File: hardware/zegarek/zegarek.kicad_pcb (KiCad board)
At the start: 2 copper layers, 123.5 x 51 mm, 15 parts, among them J1 Conn_01x02_Socket, J2 Conn_01x02_Pin, Q1 IRF740, U1 MC34063AD

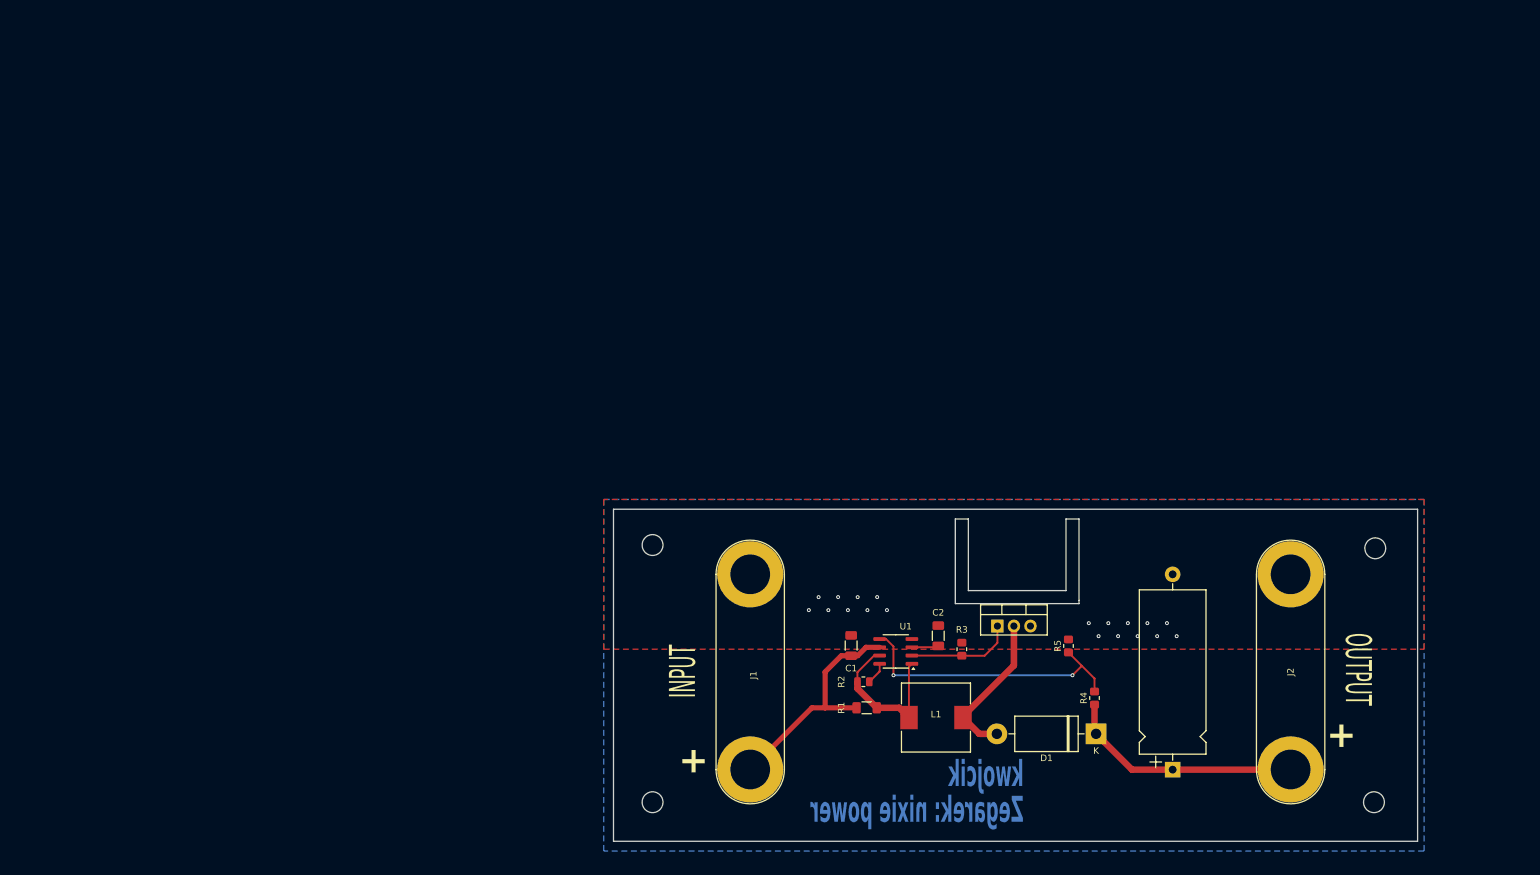
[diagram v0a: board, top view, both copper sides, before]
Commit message: done placing footprins on pcb, started tracing pcb
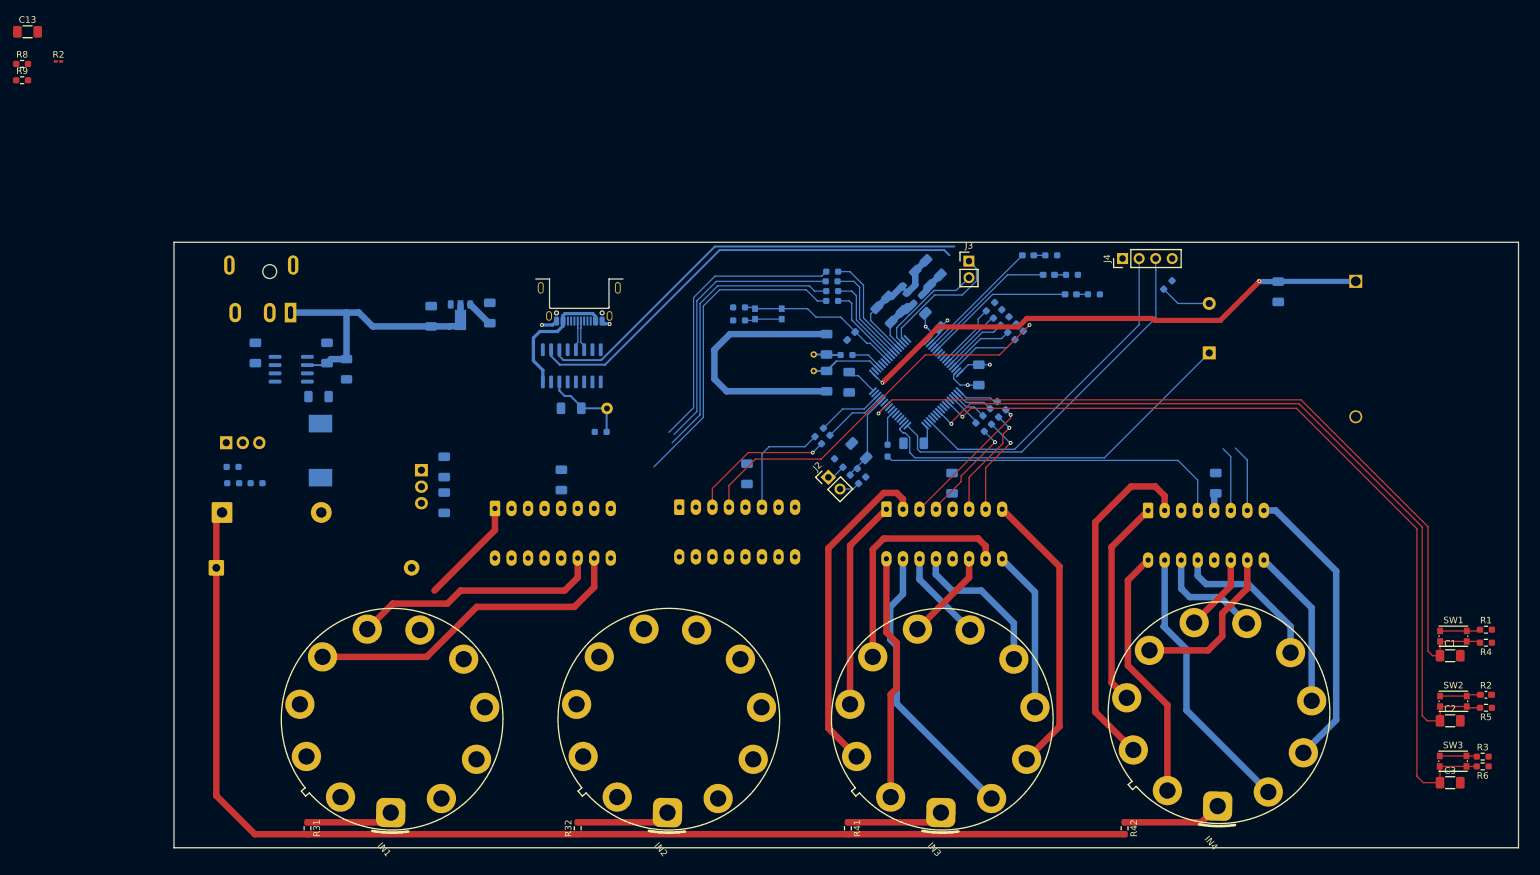
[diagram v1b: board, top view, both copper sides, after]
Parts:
- removed the R2 at (130.9, 101.0)
- removed REF**: SINK, Heatsink:SINK
- added BT1: Battery_Cell, Battery:BatteryHolder_MYOUNG_BS-07-A1BJ001_CR2032, B.Cu at (206.5, 39.5)
- added BZ1: Buzzer, Buzzer_Beeper:MagneticBuzzer_StarMicronics_HMB, B.Cu at (184.0, 50.5)
- added C10: 4u7 250V, Capacitor_THT:CP_Axial_L25.0mm_D10.0mm_P30.00mm_Horizontal, B.Cu at (31.5, 83.5)
- added C11: 10u, Capacitor_SMD:C_1206_3216Metric_Pad1.33x1.80mm_HandSolder, B.Cu at (140.0, 39.0)
- added C12: 100n, Capacitor_SMD:C_1206_3216Metric_Pad1.33x1.80mm_HandSolder, B.Cu at (141.6, 37.4)
- added C13: 100n, Capacitor_SMD:C_1206_3216Metric_Pad1.33x1.80mm_HandSolder, F.Cu at (2.50, 1.18)
- added C13: 100n, Capacitor_SMD:C_0603_1608Metric_Pad1.08x0.95mm_HandSolder, B.Cu at (129.0, 47.9)
- added C14: 100n, Capacitor_SMD:C_1206_3216Metric_Pad1.33x1.80mm_HandSolder, B.Cu at (130.2, 65.5)
- added C15: 10u, Capacitor_SMD:C_1206_3216Metric_Pad1.33x1.80mm_HandSolder, B.Cu at (134.0, 44.7)
- added C16: 100n, Capacitor_SMD:C_1206_3216Metric_Pad1.33x1.80mm_HandSolder, B.Cu at (135.7, 43.0)
- added C17: 4.3p, Capacitor_SMD:C_1206_3216Metric_Pad1.33x1.80mm_HandSolder, B.Cu at (125.2, 54.8)
- added C18: 4.3p, Capacitor_SMD:C_1206_3216Metric_Pad1.33x1.80mm_HandSolder, B.Cu at (125.2, 49.2)
- added C19: 100n, Capacitor_SMD:C_1206_3216Metric_Pad1.33x1.80mm_HandSolder, B.Cu at (194.6, 41.1)
- added C20: 100n, Capacitor_SMD:C_1206_3216Metric_Pad1.33x1.80mm_HandSolder, B.Cu at (128.7, 55.0)
- added C21: 100n, Capacitor_SMD:C_1206_3216Metric_Pad1.33x1.80mm_HandSolder, B.Cu at (138.6, 64.4)
- added C22: 100n, Capacitor_SMD:C_1206_3216Metric_Pad1.33x1.80mm_HandSolder, B.Cu at (141.5, 45.5)
- added C23: 100n, Capacitor_SMD:C_1206_3216Metric_Pad1.33x1.80mm_HandSolder, B.Cu at (148.6, 53.9)
- added C24: 100n, Capacitor_SMD:C_1206_3216Metric_Pad1.33x1.80mm_HandSolder, B.Cu at (86.0, 59.0)
- added C25: 100n, Capacitor_SMD:C_1206_3216Metric_Pad1.33x1.80mm_HandSolder, B.Cu at (84.5, 70.0)
- added C26: 100n, Capacitor_SMD:C_1206_3216Metric_Pad1.33x1.80mm_HandSolder, B.Cu at (113.0, 69.1)
- added C27: 100n, Capacitor_SMD:C_1206_3216Metric_Pad1.33x1.80mm_HandSolder, B.Cu at (144.5, 70.5)
- added C28: 100n, Capacitor_SMD:C_1206_3216Metric_Pad1.33x1.80mm_HandSolder, B.Cu at (185.0, 70.5)
- added C4: 0.33u, Capacitor_SMD:C_1206_3216Metric_Pad1.33x1.80mm_HandSolder, B.Cu at (64.5, 44.9)
- added C5: 100n, Capacitor_SMD:C_1206_3216Metric_Pad1.33x1.80mm_HandSolder, B.Cu at (73.5, 44.4)
- added C6: 100nF, Capacitor_SMD:C_1206_3216Metric_Pad1.33x1.80mm_HandSolder, B.Cu at (48.5, 50.5)
- added C7: 1nF, Capacitor_SMD:C_1206_3216Metric_Pad1.33x1.80mm_HandSolder, B.Cu at (37.5, 50.5)
- added C8: 0.33u, Capacitor_SMD:C_1206_3216Metric_Pad1.33x1.80mm_HandSolder, B.Cu at (66.5, 68.0)
- added C9: 100n, Capacitor_SMD:C_1206_3216Metric_Pad1.33x1.80mm_HandSolder, B.Cu at (66.5, 73.5)
- added D2: LED, LED_SMD:LED_0603_1608Metric_Pad1.05x0.95mm_HandSolder, B.Cu at (156.2, 35.5)
- added D3: LED, LED_SMD:LED_0603_1608Metric_Pad1.05x0.95mm_HandSolder, B.Cu at (159.4, 38.5)
- added D4: LED, LED_SMD:LED_0603_1608Metric_Pad1.05x0.95mm_HandSolder, B.Cu at (162.7, 41.5)
- added FB1: BLM18AG121SN1, Inductor_SMD:L_0603_1608Metric_Pad1.05x0.95mm_HandSolder, B.Cu at (139.2, 42.3)
- added IN1: ~, Relay_THT:IN-14 NIXIE TUBE, F.Cu at (58.3, 121.1)
- added IN2: ~, Relay_THT:IN-14 NIXIE TUBE, F.Cu at (100.8, 121.1)
- added IN3: ~, Relay_THT:IN-14 NIXIE TUBE, F.Cu at (142.8, 121.1)
- added IN4: ~, Relay_THT:IN-14 NIXIE TUBE, F.Cu at (185.3, 120.1)
- added J3: Conn_01x02, Connector_PinHeader_2.54mm:PinHeader_1x02_P2.54mm_Vertical, F.Cu at (147.1, 36.4)
- added J4: Conn_01x04, Connector_PinHeader_2.54mm:PinHeader_1x04_P2.54mm_Vertical, F.Cu at (170.7, 36.0)
- added JP1: Jumper_2_Small_Bridged, Jumper:SolderJumper-2_P1.3mm_Bridged_RoundedPad1.0x1.5mm, B.Cu at (137.2, 40.8)
- added P1: USB_C_Plug_USB2.0, Connector_USB:USB_C_Receptacle_Amphenol_12401948E412A, B.Cu at (87.2, 40.5)
- added R10: 330, Resistor_SMD:R_0603_1608Metric_Pad0.98x0.95mm_HandSolder, B.Cu at (34.0, 68.0)
- added R11: 150k, Resistor_SMD:R_0603_1608Metric_Pad0.98x0.95mm_HandSolder, B.Cu at (34.1, 70.5)
- added R12: 1k, Resistor_SMD:R_0603_1608Metric_Pad0.98x0.95mm_HandSolder, B.Cu at (37.7, 70.5)
- added R13: 1k, Resistor_SMD:R_0603_1608Metric_Pad0.98x0.95mm_HandSolder, B.Cu at (111.8, 45.5)
- added R14: 10k, Resistor_SMD:R_0603_1608Metric_Pad0.98x0.95mm_HandSolder, B.Cu at (127.1, 67.4)
- added R15: 4k7, Resistor_SMD:R_0603_1608Metric_Pad0.98x0.95mm_HandSolder, B.Cu at (111.8, 43.5)
- added R16: 10k, Resistor_SMD:R_0603_1608Metric_Pad0.98x0.95mm_HandSolder, B.Cu at (129.5, 69.9)
- added R17: 510k, Resistor_SMD:R_0603_1608Metric_Pad0.98x0.95mm_HandSolder, B.Cu at (130.6, 68.9)
- added R18: 220, Resistor_SMD:R_0603_1608Metric_Pad0.98x0.95mm_HandSolder, B.Cu at (128.3, 50.8)
- added R19: 220, Resistor_SMD:R_0603_1608Metric_Pad0.98x0.95mm_HandSolder, B.Cu at (159.7, 35.5)
- added R2: 1k, Capacitor_SMD:C_0603_1608Metric_Pad1.08x0.95mm_HandSolder, F.Cu at (226.5, 103.0)
- added R2: 1k, Resistor_SMD:R_0201_0603Metric_Pad0.64x0.40mm_HandSolder, F.Cu at (7.25, 5.72)
- added R20: 4k7, Resistor_SMD:R_0603_1608Metric_Pad0.98x0.95mm_HandSolder, B.Cu at (90.5, 62.6)
- added R21: 220, Resistor_SMD:R_0603_1608Metric_Pad0.98x0.95mm_HandSolder, B.Cu at (162.9, 38.5)
- added R22: 220, Resistor_SMD:R_0603_1608Metric_Pad0.98x0.95mm_HandSolder, B.Cu at (166.3, 41.5)
- added R23: 100, Resistor_SMD:R_0603_1608Metric_Pad0.98x0.95mm_HandSolder, B.Cu at (124.1, 62.7)
- added R24: 100, Resistor_SMD:R_0603_1608Metric_Pad0.98x0.95mm_HandSolder, B.Cu at (154.8, 47.8)
- added R25: 100, Resistor_SMD:R_0603_1608Metric_Pad0.98x0.95mm_HandSolder, B.Cu at (126.1, 41.0)
- added R26: 100, Resistor_SMD:R_0603_1608Metric_Pad0.98x0.95mm_HandSolder, B.Cu at (126.1, 38.0)
- added R27: 100, Resistor_SMD:R_0603_1608Metric_Pad0.98x0.95mm_HandSolder, B.Cu at (125.1, 63.8)
- added R28: 100, Resistor_SMD:R_0603_1608Metric_Pad0.98x0.95mm_HandSolder, B.Cu at (153.7, 46.7)
- added R29: 100, Resistor_SMD:R_0603_1608Metric_Pad0.98x0.95mm_HandSolder, B.Cu at (126.1, 42.5)
- added R30: 100, Resistor_SMD:R_0603_1608Metric_Pad0.98x0.95mm_HandSolder, B.Cu at (126.0, 39.5)
- added R31: 15k, Resistor_SMD:R_0603_1608Metric_Pad0.98x0.95mm_HandSolder, F.Cu at (45.5, 123.5)
- added R32: 15k, Resistor_SMD:R_0603_1608Metric_Pad0.98x0.95mm_HandSolder, F.Cu at (87.0, 123.5)
- added R33: 100, Resistor_SMD:R_0603_1608Metric_Pad0.98x0.95mm_HandSolder, B.Cu at (152.1, 58.6)
- added R34: 100, Resistor_SMD:R_0603_1608Metric_Pad0.98x0.95mm_HandSolder, B.Cu at (149.9, 60.8)
- added R35: 100, Resistor_SMD:R_0603_1608Metric_Pad0.98x0.95mm_HandSolder, B.Cu at (151.0, 59.7)
- added R36: 100, Resistor_SMD:R_0603_1608Metric_Pad0.98x0.95mm_HandSolder, B.Cu at (148.8, 61.9)
- added R37: 100, Resistor_SMD:R_0603_1608Metric_Pad0.98x0.95mm_HandSolder, B.Cu at (150.4, 43.4)
- added R38: 100, Resistor_SMD:R_0603_1608Metric_Pad0.98x0.95mm_HandSolder, B.Cu at (152.6, 45.6)
- added R39: 100, Resistor_SMD:R_0603_1608Metric_Pad0.98x0.95mm_HandSolder, B.Cu at (151.5, 44.5)
- added R40: 100, Resistor_SMD:R_0603_1608Metric_Pad0.98x0.95mm_HandSolder, B.Cu at (134.6, 65.5)
- added R41: 15k, Resistor_SMD:R_0603_1608Metric_Pad0.98x0.95mm_HandSolder, F.Cu at (128.5, 123.5)
- added R42: 15k, Resistor_SMD:R_0603_1608Metric_Pad0.98x0.95mm_HandSolder, F.Cu at (171.0, 123.5)
- added R6: 4k7, Resistor_SMD:R_0603_1608Metric_Pad0.98x0.95mm_HandSolder, F.Cu at (226.0, 114.0)
- added R7: 1k, Resistor_SMD:R_0603_1608Metric_Pad0.98x0.95mm_HandSolder, B.Cu at (177.6, 40.1)
- added R8: 0R22, Resistor_SMD:R_0603_1608Metric_Pad0.98x0.95mm_HandSolder, F.Cu at (1.68, 6.11)
- added R8: 0R22, Resistor_SMD:R_1206_3216Metric_Pad1.30x1.75mm_HandSolder, B.Cu at (51.5, 53.0)
- added R9: 180, Resistor_SMD:R_0603_1608Metric_Pad0.98x0.95mm_HandSolder, F.Cu at (1.68, 8.62)
- added R9: 180, Resistor_SMD:R_1206_3216Metric_Pad1.30x1.75mm_HandSolder, B.Cu at (47.2, 57.2)
- added SW1: SW_Push, Button_Switch_SMD:SW_Push_1P1T_NO_CK_KMR2, F.Cu at (221.5, 94.0)
- added SW2: SW_Push, Button_Switch_SMD:SW_Push_1P1T_NO_CK_KMR2, F.Cu at (221.5, 104.0)
- added SW3: SW_Push, Button_Switch_SMD:SW_Push_1P1T_NO_CK_KMR2, F.Cu at (221.4, 113.2)
- added SW4: SW_Push, Button_Switch_SMD:SW_Push_1P1T_NO_CK_KMR2, B.Cu at (116.3, 44.5)
- added TP1: DEBUG RST, TestPoint:TestPoint_Loop_D2.60mm_Drill0.9mm_Beaded, B.Cu at (91.5, 59.0)
- added U2: MC34063AD, Package_SO:SOIC-8_3.9x4.9mm_P1.27mm, B.Cu at (43.0, 53.0)
- added U3: L7805ACV, Package_TO_SOT_THT:TO-220-3_Vertical, B.Cu at (63.0, 68.5)
- added U4: STM32F091RCTx, Package_QFP:LQFP-64_10x10mm_P0.5mm, B.Cu at (139.0, 55.0)
- added U5: CH340C, Package_SO:SOIC-16_3.9x9.9mm_P1.27mm, B.Cu at (86.1, 52.5)
- added U6: 74141, Package_DIP:CERDIP-16_W7.62mm_SideBrazed_LongPads, B.Cu at (74.3, 74.4)
- added U7: 74141, Package_DIP:CERDIP-16_W7.62mm_SideBrazed_LongPads, B.Cu at (102.6, 74.2)
- added U8: 74141, Package_DIP:CERDIP-16_W7.62mm_SideBrazed_LongPads, B.Cu at (134.4, 74.5)
- added U9: 74141, Package_DIP:CERDIP-16_W7.62mm_SideBrazed_LongPads, B.Cu at (174.6, 74.7)
- added Y1: 32.768kHz, Crystal:Crystal_AT310_D3.0mm_L10.0mm_Horizontal, B.Cu at (123.3, 53.3)
- C1: value 100nF -> 100n
- C2: value 1nF -> 100n
- C3: value 4u7 250V -> 100n; footprint Capacitor_THT:CP_Axial_L25.0mm_D10.0mm_P30.00mm_Horizontal -> Capacitor_SMD:C_1206_3216Metric_Pad1.33x1.80mm_HandSolder
- D1, L1, Q1: moved to B.Cu
- J1: value Conn_01x02_Socket -> Barrel_Jack_MountingPin; footprint Connector:Banana_Jack_2Pin -> Connector_BarrelJack:BarrelJack_CUI_PJ-079BH_Horizontal; moved to B.Cu
- J2: value Conn_01x02_Pin -> Conn_01x02; footprint Connector:Banana_Jack_2Pin -> Connector_PinHeader_2.54mm:PinHeader_1x02_P2.54mm_Vertical
- R1: value 0R22 -> 1k; footprint Resistor_SMD:R_1206_3216Metric_Pad1.30x1.75mm_HandSolder -> Resistor_SMD:R_0603_1608Metric_Pad0.98x0.95mm_HandSolder
- R3: value 330 -> 1k; footprint Resistor_SMD:R_0805_2012Metric_Pad1.20x1.40mm_HandSolder -> Resistor_SMD:R_0603_1608Metric_Pad0.98x0.95mm_HandSolder
- R4: value 150k -> 4k7; footprint Resistor_SMD:R_0805_2012Metric_Pad1.20x1.40mm_HandSolder -> Resistor_SMD:R_0603_1608Metric_Pad0.98x0.95mm_HandSolder
- R5: value 1k -> 4k7; footprint Resistor_SMD:R_0805_2012Metric_Pad1.20x1.40mm_HandSolder -> Resistor_SMD:R_0603_1608Metric_Pad0.98x0.95mm_HandSolder
- U1: value MC34063AD -> DI78L3.3UAB; footprint Package_SO:SOIC-8_3.9x4.9mm_P1.27mm -> Package_TO_SOT_SMD:SOT-89-3; moved to B.Cu
- moved D1 138.5 mm to (32.4, 75.0), turned to 0 degrees
- moved Q1 121.7 mm to (33.0, 64.3)
- moved L1 103.0 mm to (47.5, 65.5), turned to -90 degrees
- moved R1 95.9 mm to (226.5, 93.0), turned to 0 degrees
- moved C1 92.0 mm to (221.0, 97.0), turned to 0 degrees
- moved U1 84.3 mm to (69.0, 45.0), turned to -90 degrees
- moved R3 81.7 mm to (226.0, 112.5), turned to 0 degrees
- moved J1 81.2 mm to (42.9, 44.3), turned to 0 degrees
- moved C2 79.7 mm to (221.0, 107.0), turned to 0 degrees
- moved J2 72.5 mm to (125.5, 69.6), turned to 45 degrees
- moved R5 64.8 mm to (226.5, 105.0), turned to 180 degrees
- moved R4 60.7 mm to (226.5, 95.0), turned to 180 degrees
- moved C3 42.7 mm to (221.0, 116.5), turned to 0 degrees
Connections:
- C1 pad 1: GND -> /MCU/BTNOK
- C1 pad 2: +12V -> GND
- C2 pad 1: Net-(U1-TC) -> /MCU/BTNUP
- C3 pad 1: +VDC -> /MCU/BTNDN
- D1 pad 1: +VDC -> +100V
- J1 pad 1: GND -> +12V
- J1 pad 2: +12V -> GND
- J2 pad 1: GND -> Net-(J2-Pin_1)
- J2 pad 2: +VDC -> Net-(J2-Pin_2)
- L1 pad 1: Net-(U1-Ipk) -> Net-(U2-Ipk)
- R1 pad 1: Net-(U1-Ipk) -> Net-(R1-Pad1)
- R1 pad 2: +12V -> GND
- R3 pad 1: Net-(Q1-G) -> Net-(R3-Pad1)
- R4 pad 1: +VDC -> +3V3
- R4 pad 2: Net-(U1-Vfb) -> /MCU/BTNOK
- R5 pad 1: Net-(U1-Vfb) -> +3V3
- R5 pad 2: GND -> /MCU/BTNUP
- U1 pad 1: Net-(U1-Ipk) -> GND
- U1 pad 2: Net-(Q1-G) -> +12V
- U1 pad 3: Net-(U1-TC) -> +3V3
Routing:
- net +100V: track 0.00 -> 185.8 mm
- net /MCU/BTNDN: track 0.00 -> 131.3 mm, vias 0 -> 1
- net /MCU/BTNOK: track 0.00 -> 124.8 mm, vias 0 -> 1
- net /MCU/BTNUP: track 0.00 -> 124.7 mm, vias 0 -> 1
- net /MCU/DEBUG_RX: track 0.00 -> 90.6 mm
- net /MCU/DEBUG_TX: track 0.00 -> 86.2 mm
- net +BATT: track 0.00 -> 81.5 mm, vias 0 -> 2
- net GND: track 0.00 -> 61.8 mm, vias 19 -> 4
- net Net-(U7-D): track 0.00 -> 61.1 mm, vias 0 -> 1
- net /MCU/TCK: track 0.00 -> 58.7 mm
- net /MCU/BUZZER: track 0.00 -> 58.6 mm
- net Net-(U9-D): track 0.00 -> 53.8 mm
- net Net-(IN4-K_9): track 0.00 -> 53.2 mm
- net /MCU/TMS: track 0.00 -> 52.1 mm
- net Net-(IN3-K_9): track 0.00 -> 50.7 mm
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- removed copper zone on B.Cu, net GND
- removed copper zone on F.Cu, net GND
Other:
- board size 123.5 x 51 mm -> 206.5 x 93 mm
- copper layers 2 -> 4
- board text removed: "+"
- board text removed: "INPUT"
- board text removed: "OUTPUT"
- board text removed: "Zegarek: nixie power"
- board text removed: "kwojcik"

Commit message: signal traces done
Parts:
- removed the C13 at (2.50, 1.18)
- removed the R2 at (7.25, 5.72)
- removed the R8 at (1.68, 6.11)
- removed the R9 at (1.68, 8.62)
- R40: footprint Resistor_SMD:R_0603_1608Metric_Pad0.98x0.95mm_HandSolder -> Resistor_SMD:R_1206_3216Metric_Pad1.30x1.75mm_HandSolder
- moved R40 42.8 mm to (177.4, 66.3), turned to 180 degrees
- moved C5 2.87 mm to (73.7, 41.5)
- moved C8 1.68 mm to (68.1, 68.5), turned to 0 degrees
- moved C9 1.65 mm to (68.1, 73.1), turned to 0 degrees
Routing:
- net Net-(U7-C): track 0.00 -> 57.9 mm, vias 0 -> 1
- net Net-(IN1-K_0): track 0.00 -> 51.0 mm
- net Net-(IN1-K_2): track 0.00 -> 49.4 mm
- net Net-(U9-A): track 0.00 -> 48.2 mm, vias 0 -> 2
- net Net-(IN2-K_9): track 0.00 -> 46.8 mm
- net Net-(U9-C): track 10.4 -> 54.7 mm, vias 0 -> 2
- net Net-(U9-D): track 53.8 -> 9.75 mm
- net Net-(IN2-K_2): track 0.00 -> 43.9 mm
- net Net-(U9-B): track 9.99 -> 53.8 mm, vias 0 -> 2
- net /MCU/HL_D: track 5.42 -> 48.3 mm
- net Net-(IN2-K_7): track 0.00 -> 42.8 mm
- net Net-(IN2-K_1): track 0.00 -> 41.6 mm
- net Net-(IN1-K_1): track 0.00 -> 41.4 mm
- net Net-(IN2-K_0): track 0.00 -> 40.9 mm
- net Net-(IN2-K_8): track 0.00 -> 37.3 mm
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
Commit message: pwr tracing done
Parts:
- added C6: 100nF, Capacitor_SMD:C_1206_3216Metric_Pad1.33x1.80mm_HandSolder, B.Cu at (47.0, 42.9)
- Q1, U3: footprint Package_TO_SOT_THT:TO-220-3_Vertical -> Package_TO_SOT_THT:TO-220-3_Horizontal_TabDown
- moved C7 15.6 mm to (38.2, 66.1), turned to -90 degrees
- moved C6 10.2 mm to (38.8, 53.8), turned to 0 degrees
- moved R12 9.80 mm to (28.2, 73.0), turned to 90 degrees
- moved C8 9.67 mm to (58.5, 69.7), turned to -90 degrees
- moved U2 7.99 mm to (38.8, 59.8), turned to 90 degrees
- moved R8 7.45 mm to (44.1, 53.9), turned to 180 degrees
- moved R11 6.00 mm to (29.8, 74.7), turned to 90 degrees
- moved R10 5.74 mm to (28.7, 70.2)
- moved R9 4.96 mm to (42.8, 59.5), turned to -90 degrees
- moved U3 4.46 mm to (66.1, 65.3), turned to 180 degrees
- moved C5 4.00 mm to (70.5, 39.1)
- moved C21 3.60 mm to (142.2, 64.3), turned to 0 degrees
- moved Q1 3.26 mm to (33.3, 67.5), turned to 180 degrees
- moved U1 3.08 mm to (66.8, 42.8)
- moved C4 2.75 mm to (63.1, 42.5)
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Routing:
- net +3V3: track 25.6 -> 354.3 mm, vias 2 -> 15
- net +5V: track 6.46 -> 147.5 mm, vias 0 -> 1
- net GND: track 61.8 -> 126.4 mm, vias 4 -> 35
- net Net-(IN1-K_9): track 0.00 -> 64.5 mm
- net Net-(IN1-K_8): track 0.00 -> 48.4 mm
- net Net-(U2-Vfb): track 0.00 -> 26.4 mm
- net Net-(D1-A): track 0.00 -> 25.8 mm
- net Net-(U2-Ipk): track 0.00 -> 22.9 mm
- net Net-(Q1-G): track 0.00 -> 18.2 mm
- net +12V: track 70.1 -> 78.0 mm
- net Net-(U6-A): track 76.4 -> 72.7 mm
- net +100V: track 185.8 -> 188.6 mm
- net Net-(U2-TC): track 0.00 -> 2.82 mm
- net Net-(U2-DC): track 0.00 -> 2.72 mm
- net /MCU/TCK: track 58.7 -> 61.1 mm
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- added copper zone on B.Cu, net (none)
- added copper zone on B.Cu, net GND
- added copper zone on In2.Cu, net GND
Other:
- board text added: "kwojcik bottom"
- board text added: "kwojcik top"
